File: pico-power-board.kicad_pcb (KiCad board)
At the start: 2 copper layers, 120 x 70 mm, 59 parts, among them J1 Conn_02x10_Counter_Clockwise, J10 Conn_01x07_Male, J2 Conn_02x10_Counter_Clockwise, J3 Conn_02x10_Counter_Clockwise, J4 Conn_02x10_Counter_Clockwise, J5 Conn_02x10_Counter_Clockwise, J6 Conn_02x10_Counter_Clockwise, J7 DC-053D-25A, J8 Conn_01x20_Female, J9 Conn_01x20_Female, U1 INA219AxD, U2 SN74HC541NSR, U3 K7803-500R3, U4 TMP102AIDRLR

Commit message: Update project for prototyping
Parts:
- moved R1 7.00 mm to (94.0, 95.5)
- moved R17 2.74 mm to (126.3, 136.1), turned to 0 degrees
- moved F6 2.43 mm to (193.1, 89.1)
- moved R2 2.18 mm to (94.0, 103.3)
- moved R20 1.83 mm to (141.8, 135.1)
- moved R22 1.38 mm to (156.3, 135.1)
- moved R21 1.38 mm to (150.0, 135.1)
- moved R19 1.37 mm to (137.5, 135.1)
- moved JP1 1.31 mm to (127.6, 111.7)
- moved JP2 1.14 mm to (146.0, 111.7)
- moved R18 0.86 mm to (126.3, 134.5), turned to 0 degrees
- moved F5 0.68 mm to (187.4, 89.1)
- moved R10 0.51 mm to (174.1, 103.5), turned to -90 degrees
- moved R8 0.51 mm to (153.6, 103.5), turned to -90 degrees
- moved R4 0.41 mm to (112.6, 103.4), turned to -90 degrees
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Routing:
- net +3V3: track 504.4 -> 455.6 mm, vias 3 -> 1
- net +12V: track 209.8 -> 235.0 mm
- net Net-(F1-Pad2): track 31.1 -> 24.0 mm
- net CS1_Pico: track 25.3 -> 20.7 mm
- net CS3: track 50.5 -> 46.1 mm
- net Net-(F5-Pad2): track 26.2 -> 23.5 mm
- net RESET1: track 87.4 -> 90.2 mm
- net CS2_Pico: track 31.8 -> 29.3 mm
- net CS4: track 62.9 -> 60.5 mm
- net CS6_Pico: track 47.3 -> 48.7 mm
- net CS5_Pico: track 41.5 -> 42.9 mm
- net SCK: track 153.0 -> 154.3 mm, vias 5 -> 4
- net MOSI: track 149.5 -> 150.5 mm, vias 0 -> 1
- net ADC1/I2C_SCL: track 60.7 -> 61.7 mm
- net RESET6: track 65.0 -> 64.0 mm, vias 4 -> 2
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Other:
- board text added: "pico-power-board v1"
- board text removed: "pico-power-board v0.1"

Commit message: Implement improvements from review comments
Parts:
- removed the R13 at (127.6, 97.1)
- removed R18, R19, R20, R21, R22: 10k, Resistor_SMD:R_0603_1608Metric
- J10: value Conn_01x07_Male -> Conn_01x06_Male; footprint Connector_PinSocket_2.54mm:PinSocket_1x07_P2.54mm_Vertical -> Connector_PinHeader_2.54mm:PinHeader_1x06_P2.54mm_Vertical
- R17: value 10k -> 3.3k
- moved R17 26.7 mm to (153.0, 136.7), turned to -90 degrees
- moved JP1 11.4 mm to (127.6, 100.4)
- moved U3 8.50 mm to (194.3, 127.4)
- moved JP2 6.11 mm to (146.0, 105.6)
- moved C8 5.64 mm to (192.1, 127.6), turned to 90 degrees
- moved G*** 2.51 mm to (178.2, 126.8)
- moved J10 2.32 mm to (184.8, 140.0)
- moved C1 1.93 mm to (188.7, 128.0), turned to 0 degrees
- moved C7 1.87 mm to (199.9, 133.1), turned to 0 degrees
- moved J4 1.68 mm to (203.2, 124.5)
- moved U1 0.60 mm to (187.5, 124.5)
- moved R5 0.09 mm to (133.0, 95.4)
- moved R8 0.08 mm to (153.5, 95.4)
- moved R10 0.07 mm to (174.0, 95.4)
- turned R7 to -90 degrees
- renumbered C2 to C1, C1 to C2, J7 to J4, J4 to J5, J5 to J6, J6 to J7, R9 to R10, R10 to R11, R11 to R12, R12 to R13, R15 to R14, R16 to R15, R23 to R16, R14 to R7, R7 to R8, R8 to R9, U4 to U3, U3 to U4
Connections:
- J10 pad 3: ADC2 -> I2C_SDA
- J10 pad 4: ADC0/I2C_SDA -> I2C_SCL
- J10 pad 5: ADC1/I2C_SCL -> UART0_TX
- J10 pad 6: UART0_TX -> UART0_RX
- J8 pad 11: CS3_Pico -> CS4_Pico
- J8 pad 17: CS2_Pico -> CS5_Pico
- J8 pad 20: CS1_Pico -> CS6_Pico
- J8 pad 4: CS6_Pico -> CS1_Pico
- J8 pad 6: CS5_Pico -> CS2_Pico
- J8 pad 9: CS4_Pico -> CS3_Pico
- J9 pad 10: ADC0/I2C_SDA -> I2C_SDA
- J9 pad 7: ADC2 -> ALERT
- J9 pad 9: ADC1/I2C_SCL -> I2C_SCL
- JP1 pad 2: CS2_Pico -> CS5_Pico
- JP2 pad 2: CS3_Pico -> CS4_Pico
- R15 pad 2: ADC1/I2C_SCL -> I2C_SCL
- R16 pad 2: ADC0/I2C_SDA -> I2C_SDA
- R17 pad 1: CS1_Pico -> +3V3
- R17 pad 2: +3V3 -> ALERT
- R7 pad 1: 12V_IN -> +12V
- R7 pad 2: +12V -> 12V_IN
- U1 pad 3: ADC0/I2C_SDA -> I2C_SDA
- U1 pad 4: ADC1/I2C_SCL -> I2C_SCL
- U1 pad 7: +12V -> 12V_IN
- U1 pad 8: 12V_IN -> +12V
- U2 pad 15: SCK -> CS2
- U2 pad 16: MOSI -> SCK
- U2 pad 17: CS2 -> CS1
- U2 pad 18: CS1 -> MOSI
- U2 pad 2: CS1_Pico -> MOSI_Pico
- U2 pad 3: CS2_Pico -> CS1_Pico
- U2 pad 4: MOSI_Pico -> SCK_Pico
- U2 pad 5: SCK_Pico -> CS2_Pico
- U3 pad 1: ADC1/I2C_SCL -> I2C_SCL
- U3 pad 3: ADC2 -> ALERT
- U3 pad 6: ADC0/I2C_SDA -> I2C_SDA
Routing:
- net I2C_SDA: track 0.00 -> 67.0 mm, vias 0 -> 2
- net GND: track 4.03 -> 70.4 mm, vias 0 -> 12
- net I2C_SCL: track 0.00 -> 66.2 mm, vias 0 -> 2
- net ALERT: track 0.00 -> 64.0 mm, vias 0 -> 2
- net ADC0/I2C_SDA: track 63.6 -> 0.00 mm
- net ADC1/I2C_SCL: track 61.7 -> 0.00 mm, vias 2 -> 0
- net ADC2: track 44.1 -> 0.00 mm
- net CS6_Pico: track 48.7 -> 6.74 mm, vias 1 -> 0
- net CS1_Pico: track 20.7 -> 44.2 mm
- net CS5_Pico: track 42.9 -> 29.5 mm, vias 1 -> 2
- net SCK: track 154.3 -> 144.0 mm, vias 4 -> 2
- net CS3_Pico: track 39.6 -> 29.9 mm, vias 1 -> 0
- net +3V3: track 455.6 -> 464.7 mm, vias 1 -> 0
- net CS2_Pico: track 29.3 -> 38.0 mm, vias 1 -> 0
- net CS2: track 25.2 -> 30.9 mm, vias 2 -> 0
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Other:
- board text added: "1"
- board text added: "2"
- board text added: "3"
- board text added: "4"
- board text added: "5"
- board text added: "6"
- board text added: "<-RJ45"
- board text added: "TODO: - maybe put Pico higher so it doesn't cover the screw"
- board text added: "µUSB->"
- board text removed: "ADC"
- board text removed: "RJ45"
- board text removed: "µUSB"

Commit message: Progress, I guess
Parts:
- removed JP1, JP2: Jumper_2_Open, Connector_PinHeader_2.54mm:PinHeader_1x02_P2.54mm_Vertical
- moved F3 6.14 mm to (145.9, 83.2), turned to -90 degrees
- moved F2 6.01 mm to (125.2, 83.2), turned to -90 degrees
- moved F4 5.99 mm to (166.3, 83.2), turned to -90 degrees
- moved G*** 0.74 mm to (177.5, 126.7)
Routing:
- net +12V: track 234.7 -> 213.6 mm
- net CS5_Pico: track 29.5 -> 10.1 mm, vias 2 -> 0
- net CS4_Pico: track 39.7 -> 24.3 mm, vias 1 -> 0
- net Net-(J2-Pin_10): track 24.5 -> 27.2 mm
- net Net-(J5-Pin_10): track 24.4 -> 27.1 mm
- net Net-(J3-Pin_10): track 24.9 -> 27.1 mm
- net GND: track 70.4 -> 68.7 mm, vias 12 -> 13
- net RESET6: vias 2 -> 3
- net MOSI: vias 1 -> 0
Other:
- board text added: "pico-power-board v0.1"
- board text removed: "pico-power-board v1"

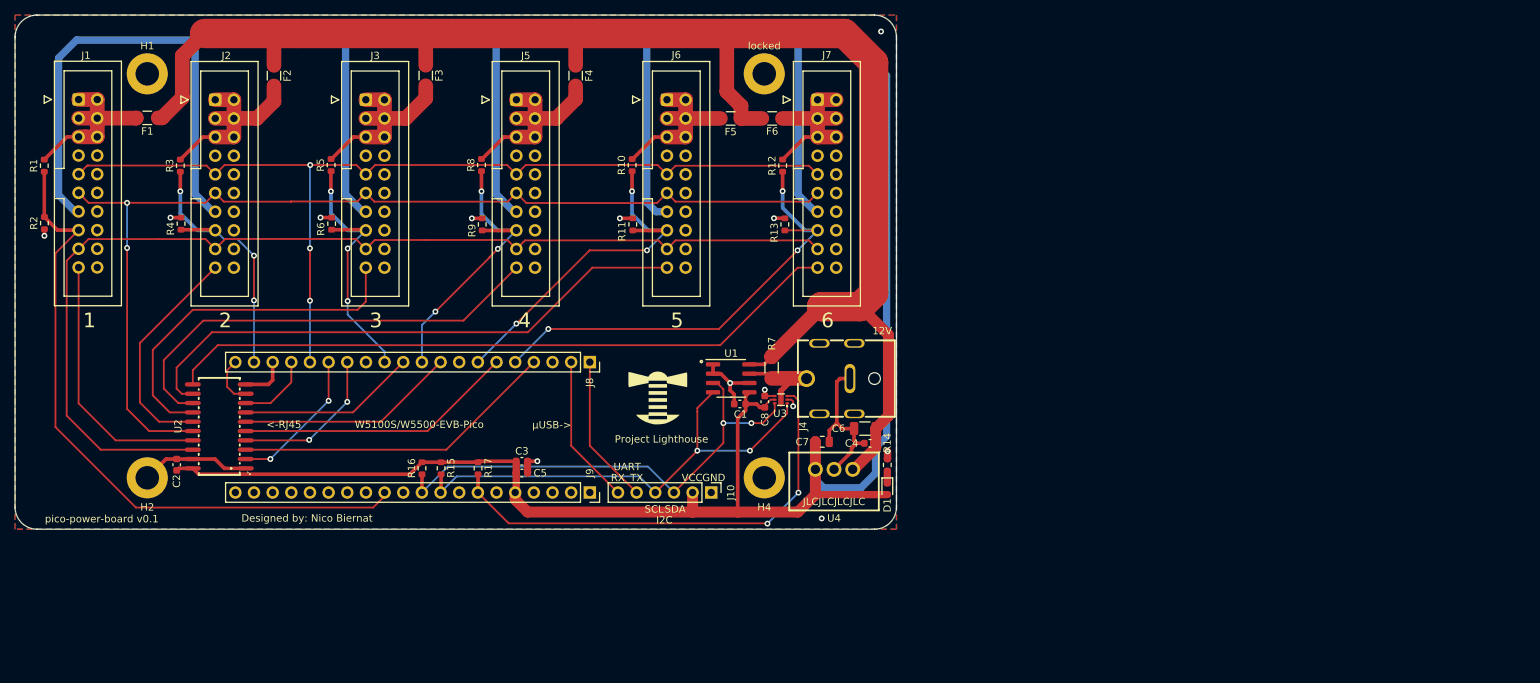
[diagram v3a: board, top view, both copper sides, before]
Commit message: Add SPI signal termination and remove line driver
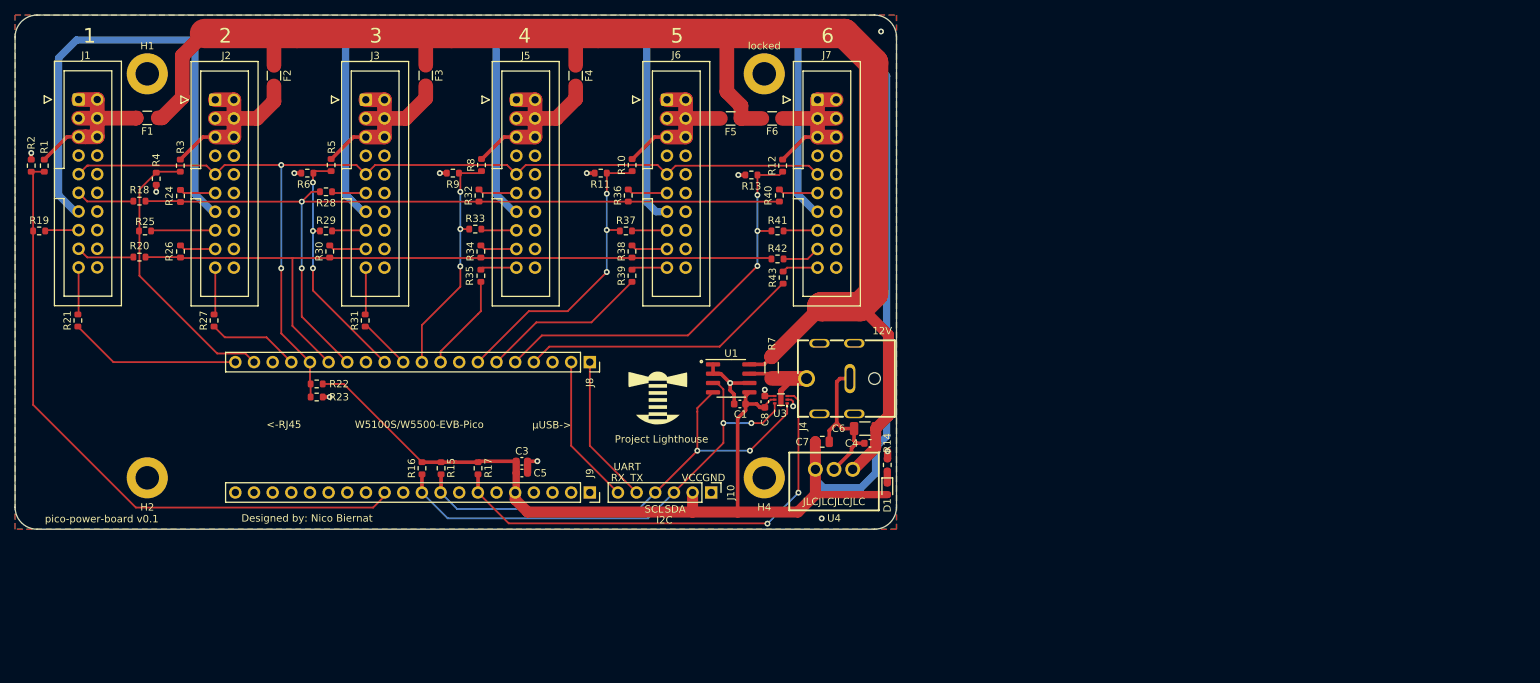
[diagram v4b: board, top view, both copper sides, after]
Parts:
- removed C2: 100nF, Capacitor_SMD:C_0603_1608Metric
- removed U2: SN74HC541NSR, Lighthouse:SOIC-20_L12.6-W5.3-P1.27-LS7.8-BL
- added R18: 100, Resistor_SMD:R_0603_1608Metric, F.Cu at (106.9, 100.3)
- added R19: 100, Resistor_SMD:R_0603_1608Metric, F.Cu at (93.3, 104.4)
- added R20: 100, Resistor_SMD:R_0603_1608Metric, F.Cu at (106.9, 108.0)
- added R21: 100, Resistor_SMD:R_0603_1608Metric, F.Cu at (98.6, 116.6)
- added R22: 200, Resistor_SMD:R_0603_1608Metric, F.Cu at (131.1, 125.2)
- added R23: 200, Resistor_SMD:R_0603_1608Metric, F.Cu at (131.1, 127.0)
- added R24: 100, Resistor_SMD:R_0603_1608Metric, F.Cu at (112.5, 99.6)
- added R25: 100, Resistor_SMD:R_0603_1608Metric, F.Cu at (107.7, 104.4)
- added R26: 100, Resistor_SMD:R_0603_1608Metric, F.Cu at (112.5, 107.2)
- added R27: 100, Resistor_SMD:R_0603_1608Metric, F.Cu at (117.1, 116.6)
- added R28: 100, Resistor_SMD:R_0603_1608Metric, F.Cu at (132.3, 99.1)
- added R29: 100, Resistor_SMD:R_0603_1608Metric, F.Cu at (132.3, 104.4)
- added R30: 100, Resistor_SMD:R_0603_1608Metric, F.Cu at (132.8, 107.2)
- added R31: 100, Resistor_SMD:R_0603_1608Metric, F.Cu at (137.7, 116.6)
- added R32: 100, Resistor_SMD:R_0603_1608Metric, F.Cu at (153.2, 99.6)
- added R33: 100, Resistor_SMD:R_0603_1608Metric, F.Cu at (152.7, 104.1)
- added R34: 100, Resistor_SMD:R_0603_1608Metric, F.Cu at (153.4, 107.2)
- added R35: 100, Resistor_SMD:R_0603_1608Metric, F.Cu at (153.4, 110.5)
- added R36: 100, Resistor_SMD:R_0603_1608Metric, F.Cu at (173.5, 99.6)
- added R37: 100, Resistor_SMD:R_0603_1608Metric, F.Cu at (173.2, 104.4)
- added R38: 100, Resistor_SMD:R_0603_1608Metric, F.Cu at (174.0, 107.2)
- added R39: 100, Resistor_SMD:R_0603_1608Metric, F.Cu at (174.0, 110.5)
- added R40: 100, Resistor_SMD:R_0603_1608Metric, F.Cu at (194.1, 99.6)
- added R41: 100, Resistor_SMD:R_0603_1608Metric, F.Cu at (193.8, 104.4)
- added R42: 100, Resistor_SMD:R_0603_1608Metric, F.Cu at (193.8, 108.2)
- added R43: 100, Resistor_SMD:R_0603_1608Metric, F.Cu at (194.6, 110.7)
- moved R11 8.23 mm to (169.7, 96.5), turned to 0 degrees
- moved R13 8.12 mm to (190.2, 96.8), turned to 0 degrees
- moved R9 8.04 mm to (149.6, 96.5), turned to 0 degrees
- moved R2 8.02 mm to (92.2, 95.5), turned to -90 degrees
- moved R6 7.63 mm to (129.8, 96.5), turned to 0 degrees
- moved R4 6.99 mm to (109.2, 97.3), turned to 90 degrees
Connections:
- J1 pad 16: SCK -> Net-(J1-Pin_16)
- J1 pad 18: RESET1 -> Net-(J1-Pin_18)
- J1 pad 19: MOSI -> Net-(J1-Pin_19)
- J1 pad 20: CS1 -> Net-(J1-Pin_20)
- J2 pad 16: SCK -> Net-(J2-Pin_16)
- J2 pad 18: RESET2 -> Net-(J2-Pin_18)
- J2 pad 19: MOSI -> Net-(J2-Pin_19)
- J2 pad 20: CS2 -> Net-(J2-Pin_20)
- J3 pad 16: SCK -> Net-(J3-Pin_16)
- J3 pad 18: RESET3 -> Net-(J3-Pin_18)
- J3 pad 19: MOSI -> Net-(J3-Pin_19)
- J3 pad 20: CS3 -> Net-(J3-Pin_20)
- J5 pad 16: SCK -> Net-(J5-Pin_16)
- J5 pad 18: RESET4 -> Net-(J5-Pin_18)
- J5 pad 19: MOSI -> Net-(J5-Pin_19)
- J5 pad 20: CS4 -> Net-(J5-Pin_20)
- J6 pad 16: SCK -> Net-(J6-Pin_16)
- J6 pad 18: RESET5 -> Net-(J6-Pin_18)
- J6 pad 19: MOSI -> Net-(J6-Pin_19)
- J6 pad 20: CS5 -> Net-(J6-Pin_20)
- J7 pad 16: SCK -> Net-(J7-Pin_16)
- J7 pad 18: RESET6 -> Net-(J7-Pin_18)
- J7 pad 19: MOSI -> Net-(J7-Pin_19)
- J7 pad 20: CS6 -> Net-(J7-Pin_20)
- J8 pad 11: CS4_Pico -> CS3
- J8 pad 14: SCK_Pico -> SCK
- J8 pad 15: MOSI_Pico -> MOSI
- J8 pad 17: CS5_Pico -> CS2
- J8 pad 20: CS6_Pico -> CS1
- J8 pad 4: CS1_Pico -> CS6
- J8 pad 6: CS2_Pico -> CS5
- J8 pad 9: CS3_Pico -> CS4
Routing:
- net CS5: track 77.7 -> 23.0 mm
- net CS6: track 92.8 -> 38.4 mm
- net CS4: track 61.9 -> 13.2 mm
- net MOSI: track 148.3 -> 101.5 mm
- net CS1_Pico: track 44.2 -> 0.00 mm
- net CS3: track 49.0 -> 7.19 mm
- net CS2_Pico: track 38.0 -> 0.00 mm
- net SCK: track 144.0 -> 113.8 mm
- net CS3_Pico: track 29.9 -> 0.00 mm
- net CS4_Pico: track 24.3 -> 0.00 mm
- net GND: track 68.7 -> 45.8 mm, vias 13 -> 14
- net SCK_Pico: track 21.4 -> 0.00 mm, vias 2 -> 0
- net MOSI_Pico: track 19.8 -> 0.00 mm, vias 2 -> 0
- net CS2: track 30.9 -> 12.5 mm
- net +3V3: track 464.7 -> 448.1 mm
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
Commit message: Refactor schematic and change temperature sensor from TMP102 to TMP112
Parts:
- U3: value TMP102AIDRLR -> TMP112AIDRLR

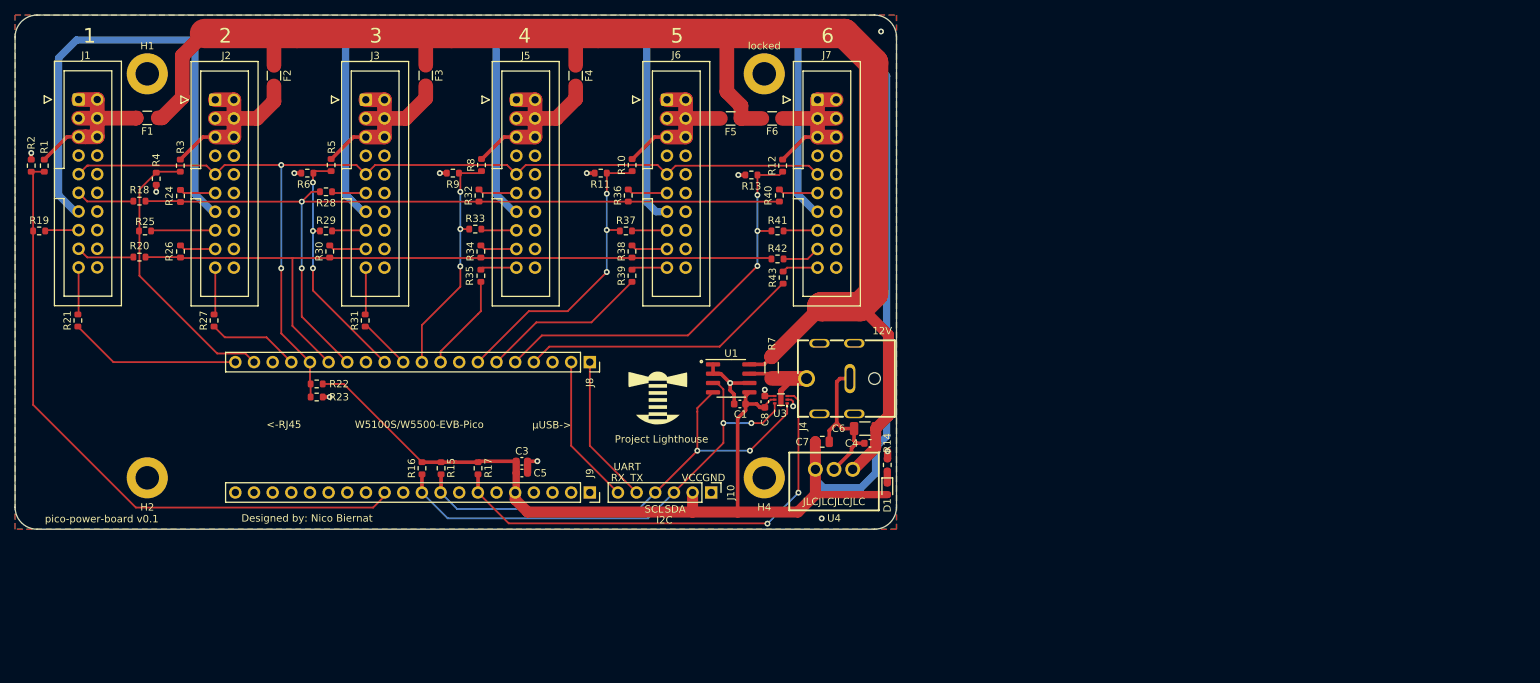
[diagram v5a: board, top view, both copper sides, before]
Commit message: Change DC-Jack to an available option, add logos and some trace refactoring
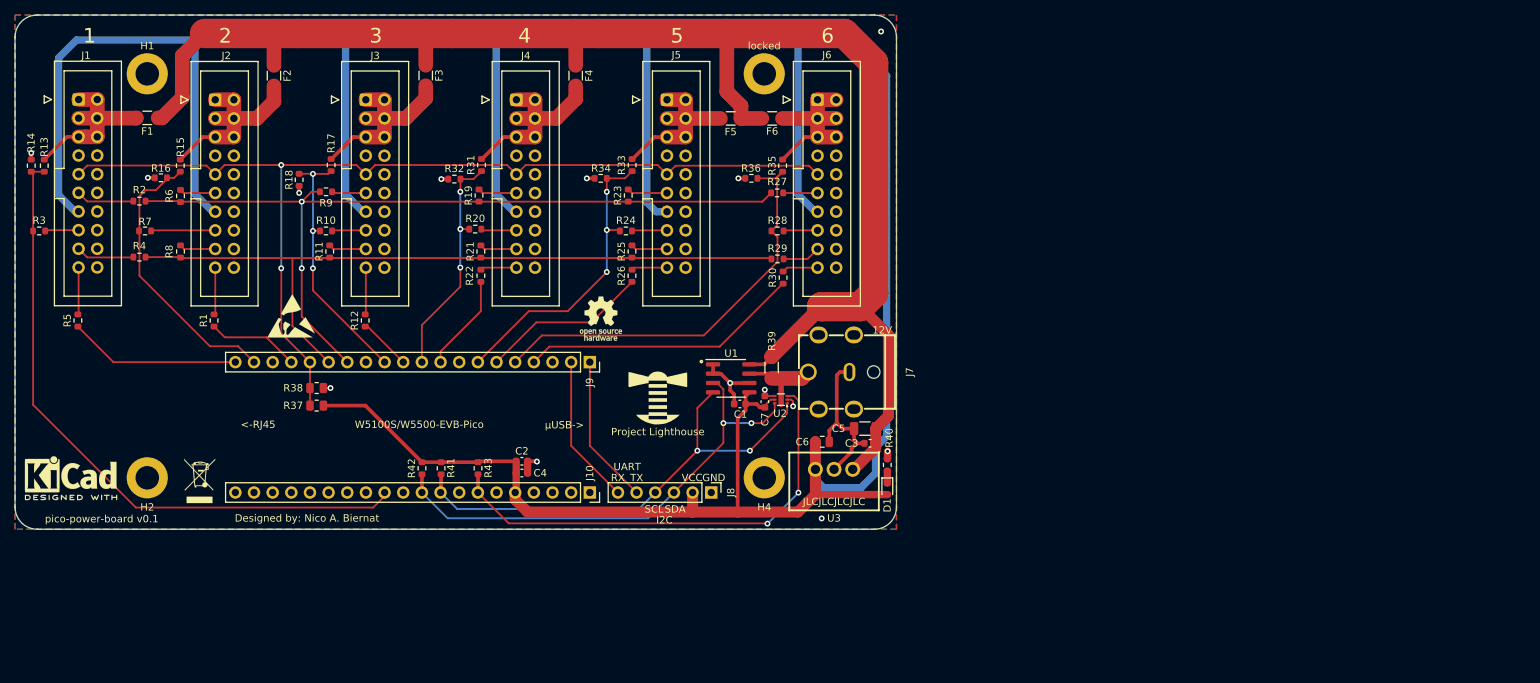
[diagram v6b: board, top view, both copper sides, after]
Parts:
- added REF**: ESD-Logo_6.6x6mm_SilkScreen, Symbol:ESD-Logo_6.6x6mm_SilkScreen, F.Cu at (127.6, 115.9)
- added REF**: OSHW-Logo_5.7x6mm_SilkScreen, Symbol:OSHW-Logo_5.7x6mm_SilkScreen, F.Cu at (169.8, 116.3)
- added REF**: KiCad-Logo2_5mm_SilkScreen, Symbol:KiCad-Logo2_5mm_SilkScreen, F.Cu at (97.6, 138.0)
- added REF**: WEEE-Logo_4.2x6mm_SilkScreen, Symbol:WEEE-Logo_4.2x6mm_SilkScreen, F.Cu at (115.1, 138.4)
- J7: renamed from J4; value DC-053D-25A -> DC-042C-Z-2.5; footprint Lighthouse:DC-IN-TH_DC-053D-25A-1 -> Lighthouse:DC-IN-TH_DC-042C-Z-2.5
- R37: renamed from R22; footprint Resistor_SMD:R_0603_1608Metric -> Resistor_SMD:R_0805_2012Metric
- R38: renamed from R23; footprint Resistor_SMD:R_0603_1608Metric -> Resistor_SMD:R_0805_2012Metric
- moved R37 2.95 mm to (131.1, 128.2)
- moved J7 2.26 mm to (201.1, 123.6)
- moved R18 1.44 mm to (128.7, 97.4), turned to 90 degrees
- moved R38 1.22 mm to (131.1, 125.8)
- moved R32 0.84 mm to (149.8, 97.3)
- moved R34 0.71 mm to (169.7, 97.2)
- moved R16 0.65 mm to (109.9, 97.2), turned to 0 degrees
- moved R27 0.47 mm to (193.8, 99.2), turned to 0 degrees
- moved R36 0.46 mm to (190.2, 97.2)
- renumbered C3 to C2, C4 to C3, C5 to C4, C6 to C5, C7 to C6, C8 to C7, J9 to J10, J5 to J4, J6 to J5, J7 to J6, J10 to J8, J8 to J9, R27 to R1, R29 to R10, R30 to R11, R31 to R12, R1 to R13, R2 to R14, R3 to R15, R4 to R16, R5 to R17, R6 to R18, R32 to R19, R18 to R2, R33 to R20, R34 to R21, R35 to R22, R36 to R23, R37 to R24, R38 to R25, R39 to R26, R40 to R27, R41 to R28, R42 to R29, R19 to R3, R43 to R30, R8 to R31, R9 to R32, R10 to R33, R11 to R34, R12 to R35, R13 to R36, R7 to R39, R20 to R4, R14 to R40, R15 to R41, R16 to R42, R17 to R43, R21 to R5, R24 to R6, R25 to R7, R26 to R8, R28 to R9, U3 to U2, U4 to U3
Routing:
- net RESET6: track 56.3 -> 58.4 mm, vias 3 -> 0
- net RESET3: track 33.3 -> 35.1 mm
- net 12V_IN: track 14.0 -> 12.2 mm
- net +3V3: track 448.1 -> 446.7 mm
- net MISO: track 139.0 -> 140.1 mm
- net RESET4: track 32.4 -> 31.6 mm
- net Net-(J6-Pin_16): track 5.40 -> 4.68 mm
- net SCK: track 113.8 -> 113.2 mm
- net GND: track 45.8 -> 46.5 mm
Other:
- board text added: "Designed by: Nico A. Biernat"
- board text removed: "Designed by: Nico Biernat"
- board text removed: "Project Lighthouse"
